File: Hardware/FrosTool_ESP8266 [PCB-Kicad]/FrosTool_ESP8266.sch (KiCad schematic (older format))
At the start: 28 parts, among them J1 IN_PANEL, J10 V3.3, J11 V3.3, J12 V3.3, J13 GND, J14 GND, J15 GND, J2 BATERIA, J3 TX_RX, J4 GPIO13(D)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

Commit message: Tracks and Vias improvement Bug Fixed: Pads Regulator
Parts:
- removed U1: AP1117-33, TO_SOT_Packages_SMD:SOT89-3_Housing, symbol AP1117-33
- added U1: HT7333-1, TO_SOT_Packages_SMD:SOT89-3_Housing, symbol HT7333-1
- C2: footprint Capacitors_SMD:c_elec_3x5.3 -> Capacitors_SMD:c_elec_4x5.3
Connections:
- net +3V3: now also U1.3 (VO)
- net BAT+: now also U1.2 (VI)
- net GND: now also U1.1 (GND)
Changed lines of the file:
@@
 LIBS:tp4056
 LIBS:switches
+LIBS:ht7333-1
 LIBS:FrosTool_ESP8266-cache
 EELAYER 25 0
@@
 $EndComp
 $Comp
-L AP1117-33 U1
-U 1 1 59D43096
-P 3250 1400
-F 0 "U1" H 3100 1525 50  0000 C CNN
-F 1 "AP1117-33" H 3250 1525 50  0000 L CNN
-F 2 "TO_SOT_Packages_SMD:SOT89-3_Housing" H 3250 1600 50  0001 C CNN
-F 3 "" H 3350 1150 50  0001 C CNN
-	1    3250 1400
-	1    0    0    -1
-$EndComp
-$Comp
 L Conn_01x01 J5
 U 1 1 59D43147
@@
 F 0 "C2" H 4125 1650 50  0000 L CNN
 F 1 "10uF" H 4125 1450 50  0000 L CNN
-F 2 "Capacitors_SMD:c_elec_3x5.3" H 4138 1400 50  0001 C CNN
+F 2 "Capacitors_SMD:c_elec_4x5.3" H 4138 1400 50  0001 C CNN
 F 3 "" H 4100 1550 50  0001 C CNN
 	1    4100 1550
@@
 Wire Notes Line
 	1100 6100 1100 3500
+$Comp
+L HT7333-1 U1
+U 1 1 59E17844
+P 3250 1400
+F 0 "U1" H 3100 1525 50  0000 C CNN
+F 1 "HT7333-1" H 3250 1525 50  0000 L CNN
+F 2 "TO_SOT_Packages_SMD:SOT89-3_Housing" H 3250 1600 50  0001 C CNN
+F 3 "" H 3350 1150 50  0001 C CNN
+	1    3250 1400
+	1    0    0    -1
+$EndComp
 $EndSCHEMATC

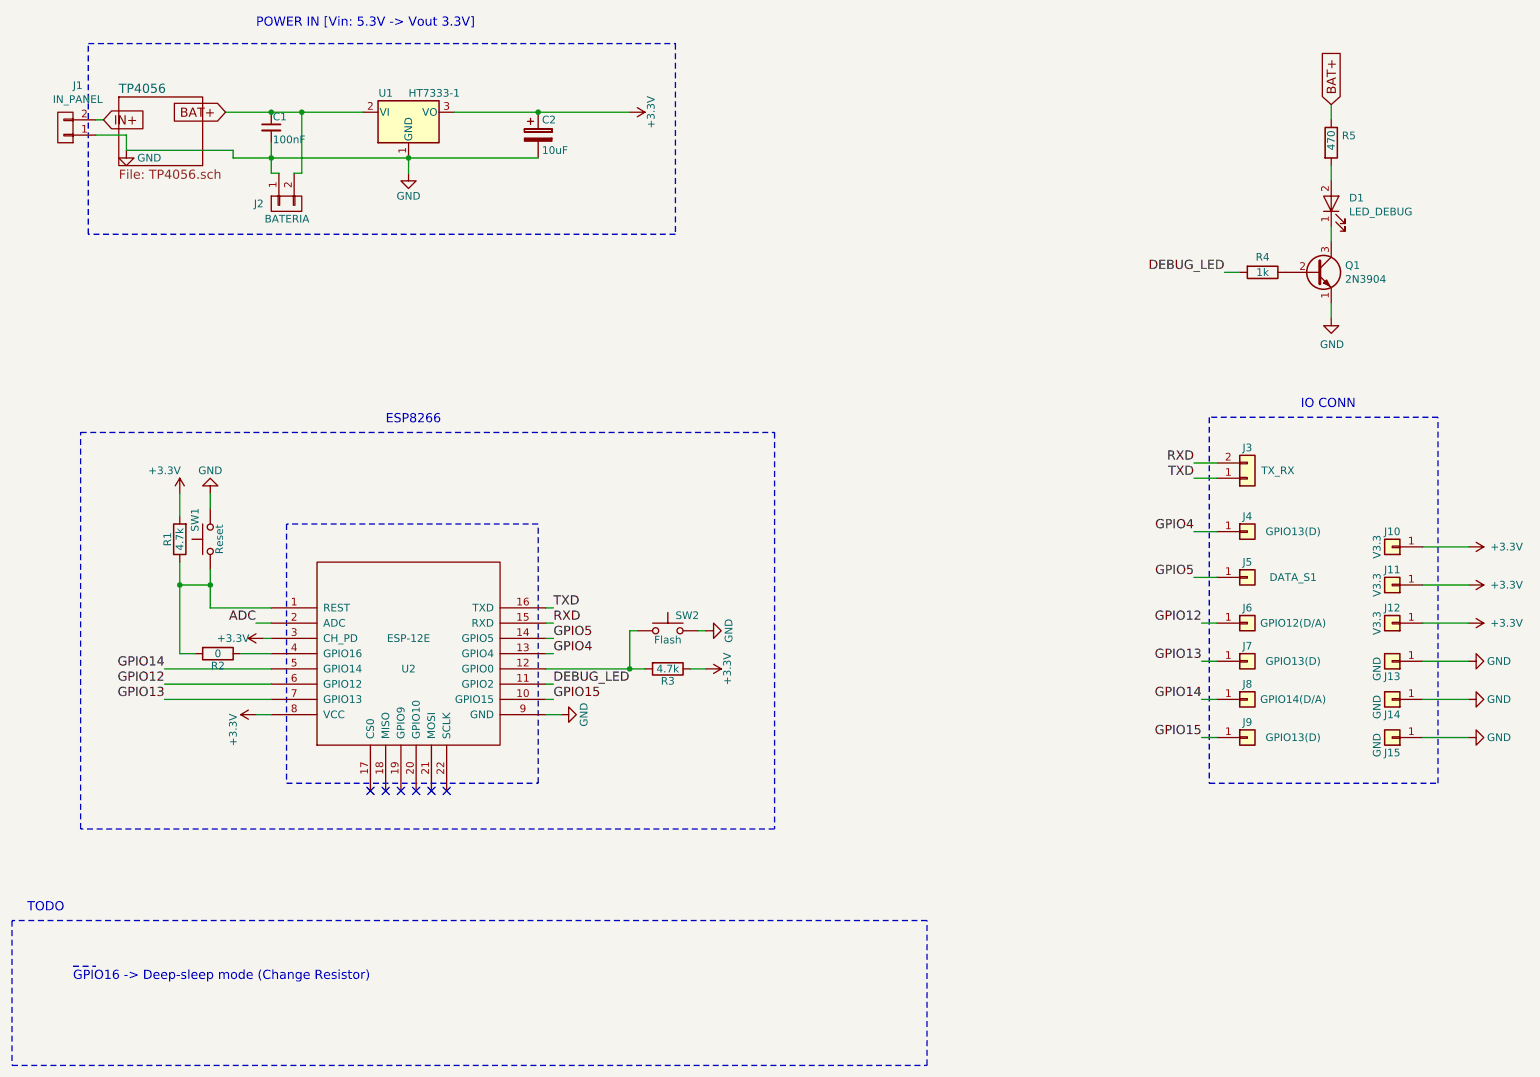
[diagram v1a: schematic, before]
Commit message: F.Fab, B.Fab
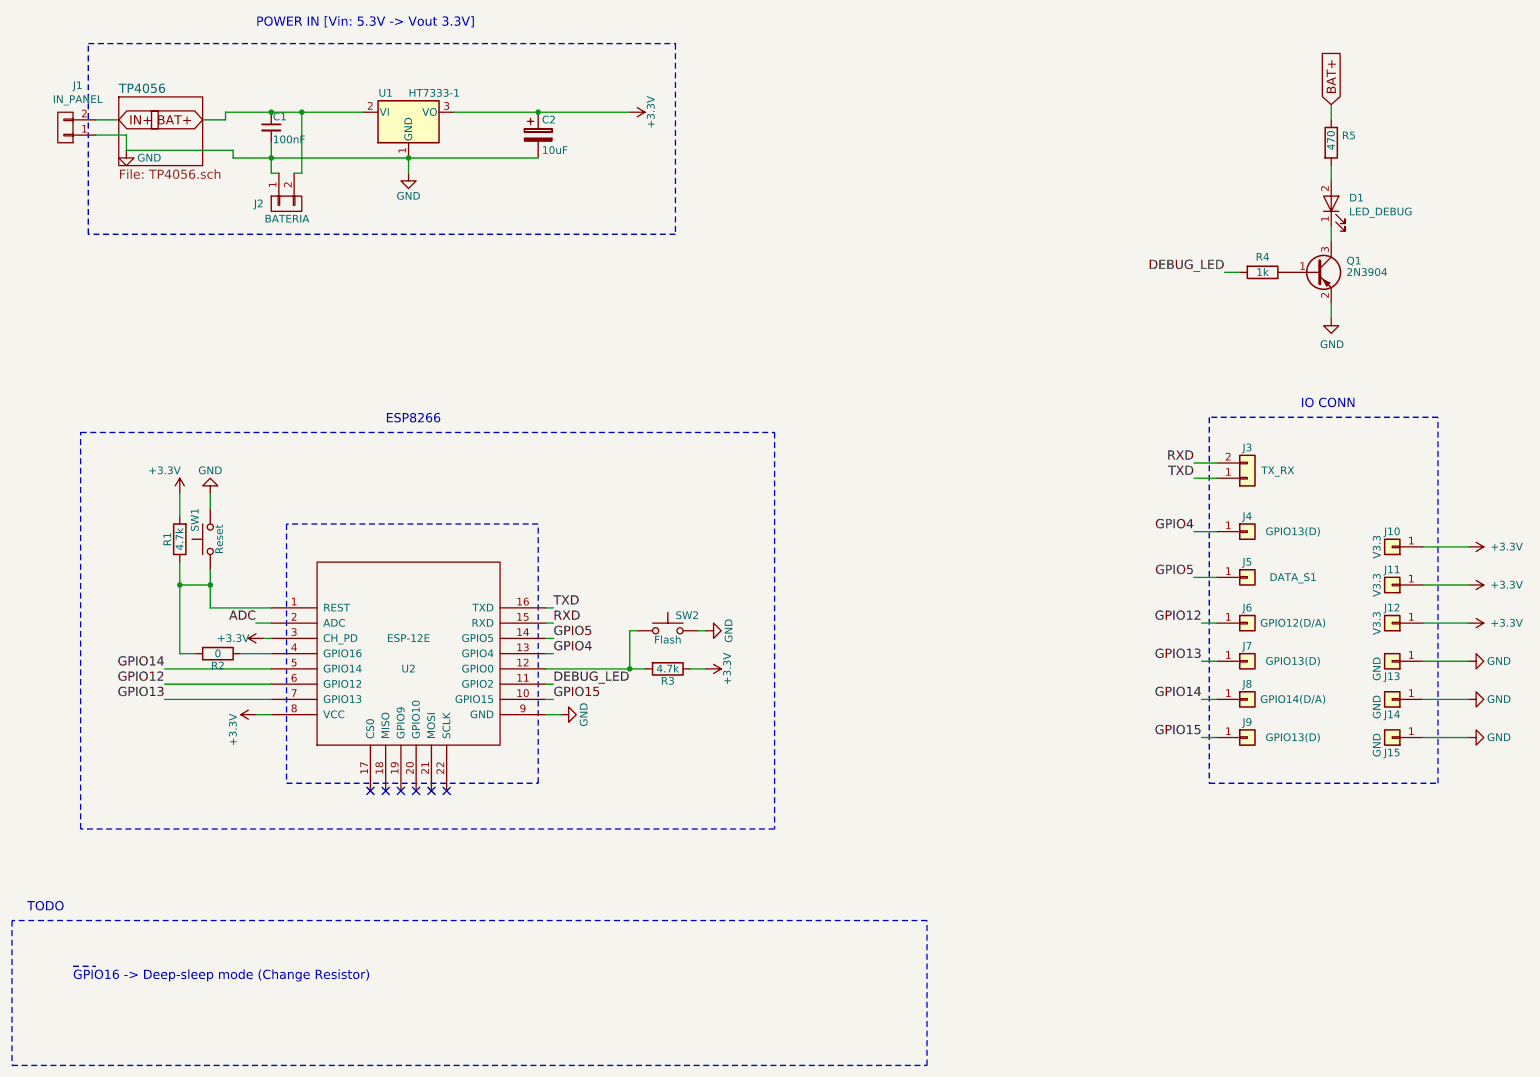
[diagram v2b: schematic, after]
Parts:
- removed Q1: 2N3904, TO_SOT_Packages_SMD:SOT-23, symbol 2N3904
- added Q1: 2N3904, TO_SOT_Packages_SMD:SOT-23, symbol BC807
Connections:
- net GND: now also Q1.2 (E)
- net at R4.1: now also Q1.1 (B)
- net at D1.1 (K): now also Q1.3 (C)
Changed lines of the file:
@@
-$EndComp
-$Comp
-L 2N3904 Q1
-U 1 1 59D831CB
-P 9200 2450
-F 0 "Q1" H 9391 2496 50  0000 L CNN
-F 1 "2N3904" H 9391 2405 50  0000 L CNN
-F 2 "TO_SOT_Packages_SMD:SOT-23" H 9400 2375 50  0001 L CIN
-F 3 "" H 9200 2450 50  0001 L CNN
-	1    9200 2450
-	1    0    0    -1
 $EndComp
 $Comp
@@
 	1    0    0    -1
 $EndComp
-Text GLabel 1250 1450 2    60   Input ~ 0
+Text GLabel 1350 1450 2    60   Input ~ 0
 IN+
-Text GLabel 2050 1400 0    60   Input ~ 0
+Text GLabel 1900 1450 0    60   Input ~ 0
 BAT+
 Wire Wire Line
@@
 	1950 3900 1950 4000
 Wire Wire Line
-	1950 4650 1950 4400
+	1950 4400 1950 4650
 Wire Wire Line
 	1750 4050 1750 3900
@@
 Connection ~ 1950 4500
 Wire Wire Line
-	2350 4650 1950 4650
+	1950 4650 2350 4650
 Wire Wire Line
 	8400 3700 8550 3700
@@
 Wire Wire Line
 	2050 1400 2950 1400
-Wire Wire Line
-	1250 1450 1200 1450
 $Sheet
 S 1350 1300 550  450
@@
 	1    0    0    -1
 $EndComp
+$Comp
+L BC807 Q1
+U 1 1 59E3AC14
+P 9200 2450
+F 0 "Q1" H 9400 2525 50  0000 L CNN
+F 1 "2N3904" H 9400 2450 50  0000 L CNN
+F 2 "TO_SOT_Packages_SMD:SOT-23" H 9400 2375 50  0001 L CIN
+F 3 "" H 9200 2450 50  0001 L CNN
+	1    9200 2450
+	1    0    0    -1
+$EndComp
+Wire Wire Line
+	1200 1450 1350 1450
+Wire Wire Line
+	1900 1450 2050 1450
+Wire Wire Line
+	2050 1450 2050 1400
 $EndSCHEMATC

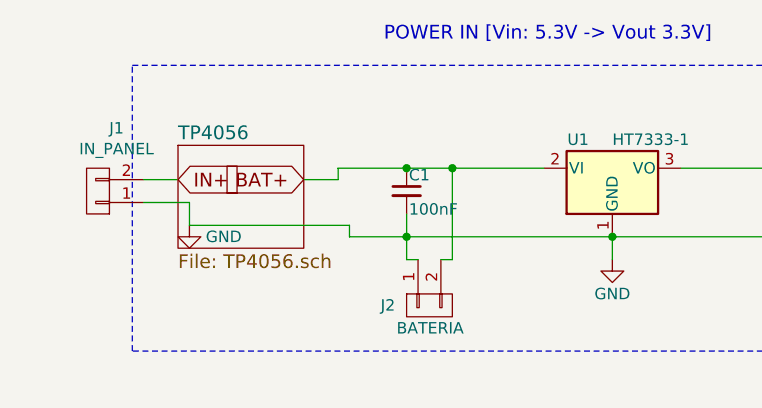
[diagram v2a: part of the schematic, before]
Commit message: Added Pin Extra: BAT+
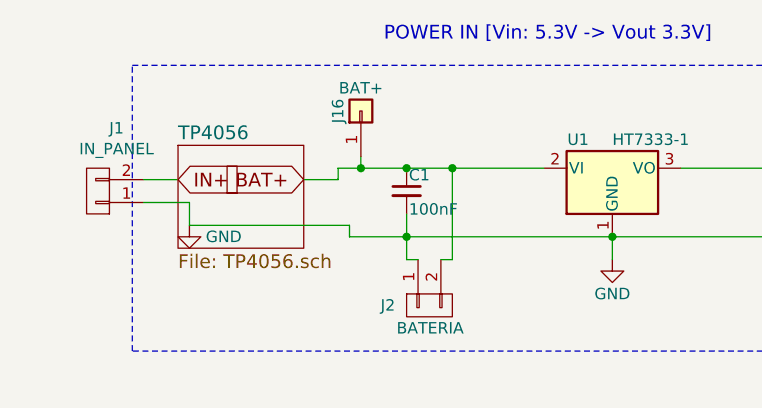
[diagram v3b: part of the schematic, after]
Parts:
- added J16: BAT+, Pin_Headers:Pin_Header_Straight_1x01, symbol Conn_01x01
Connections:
- net BAT+: now also J16.1 (Pin_1)
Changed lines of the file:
@@
 Wire Wire Line
 	2050 1450 2050 1400
+$Comp
+L Conn_01x01 J16
+U 1 1 59E55F20
+P 2150 1150
+F 0 "J16" H 2150 1250 50  0000 C CNN
+F 1 "BAT+" V 2250 1150 50  0000 C CNN
+F 2 "Pin_Headers:Pin_Header_Straight_1x01" H 2150 1150 50  0001 C CNN
+F 3 "" H 2150 1150 50  0001 C CNN
+	1    2150 1150
+	0    -1   -1   0
+$EndComp
+Wire Wire Line
+	2150 1350 2150 1400
+Connection ~ 2150 1400
 $EndSCHEMATC

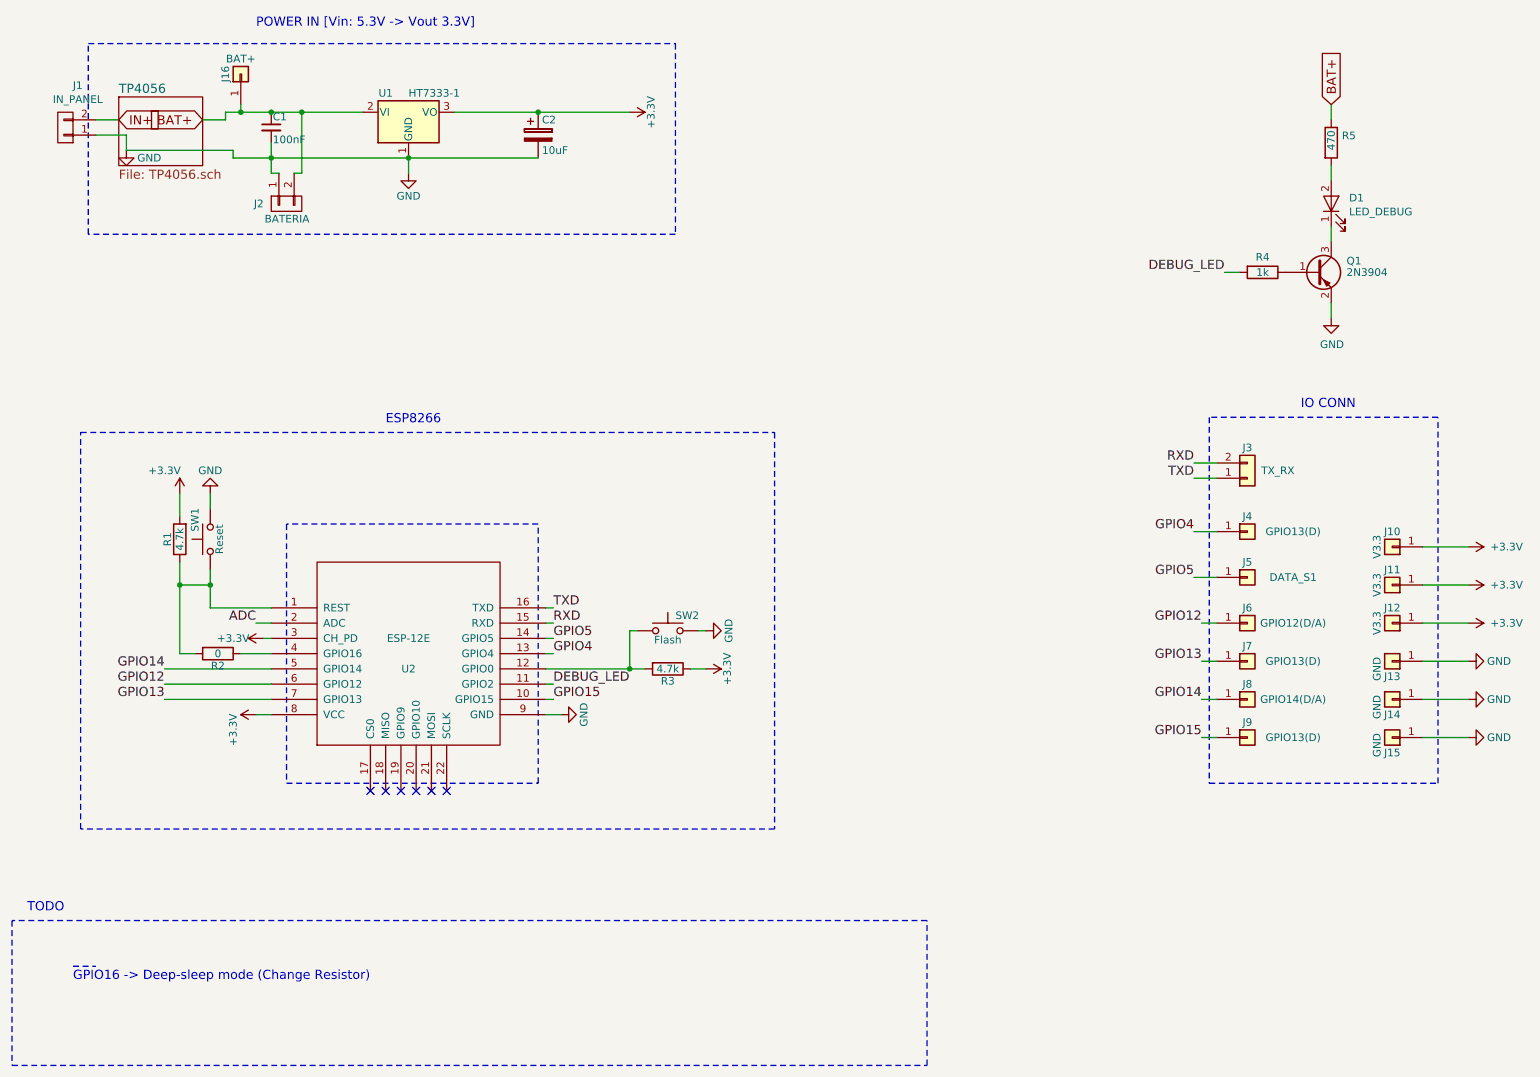
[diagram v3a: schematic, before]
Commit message: Bug Fixed (R10k x2), No Programing, Debug_led(USERLED)
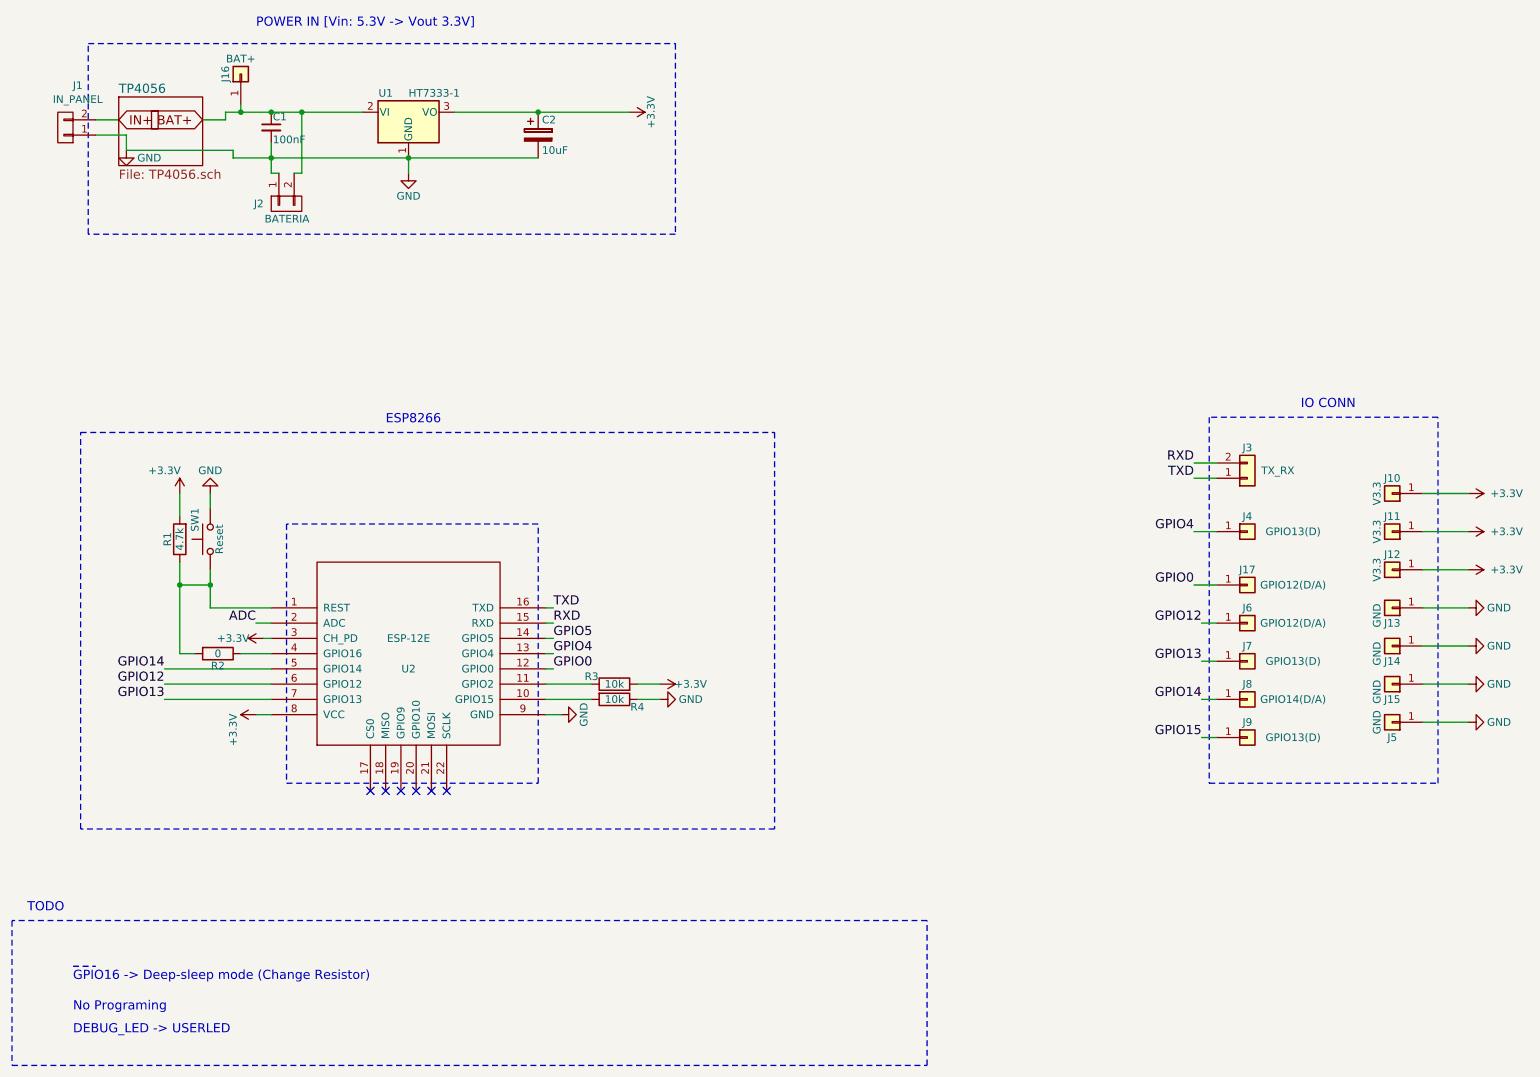
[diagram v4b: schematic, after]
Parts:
- removed D1: LED_DEBUG, LEDs:LED-3MM, symbol LED
- removed Q1: 2N3904, TO_SOT_Packages_SMD:SOT-23, symbol BC807
- removed R5: 470, Resistors_SMD:R_1206, symbol R
- removed SW2: Flash, Buttons_Switches_SMD:SW_SPST_B3U-1000P, symbol SW_Push
- added J17: GPIO12(D/A), Pin_Headers:Pin_Header_Straight_1x01, symbol Conn_01x01
- J5: value DATA_S1 -> GND
- R3: value 4.7k -> 10k; footprint Resistors_SMD:R_1206 -> (none)
- R4: value 1k -> 10k; footprint Resistors_SMD:R_1206 -> (none)
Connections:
- net +3V3: now also R3.2; no longer R3.1
- net GND: now also J5.1 (Pin_1), R4.1
- net GPIO15: no longer U2.10 (GPIO15)
- net GPIO5: no longer J5.1 (Pin_1)
- net GPIO0: now reaches U2.12 (GPIO0)
- net GPIO0: now also J17.1 (Pin_1); no longer R3.2
- net DEBUG_LED: no longer names the net of R4.2
- net DEBUG_LED: now also U2.10 (GPIO15); no longer U2.11 (GPIO2)
- new net: R3.1, U2.11 (GPIO2)
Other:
- note added: "DEBUG_LED -> USERLED"
- note added: "No Programing"
- moved on the sheet: J10, J11, J12, J13, J14, J15, J5
